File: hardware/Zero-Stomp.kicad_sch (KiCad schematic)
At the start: 90 parts, among them J1 Power, J2 Left Input, J3 Right Input, J4 Expression, J5 Left Output, J6 Right Output, J7 MIDI_IN, J8 MIDI_OUT, U1 L78L05_TO92, U2 H11L1, U3 RP2040-Zero, U4 WM8960CGEFL/V, U5 TL972, U6 SSD1306-OLED-SPI, X1 24MHz

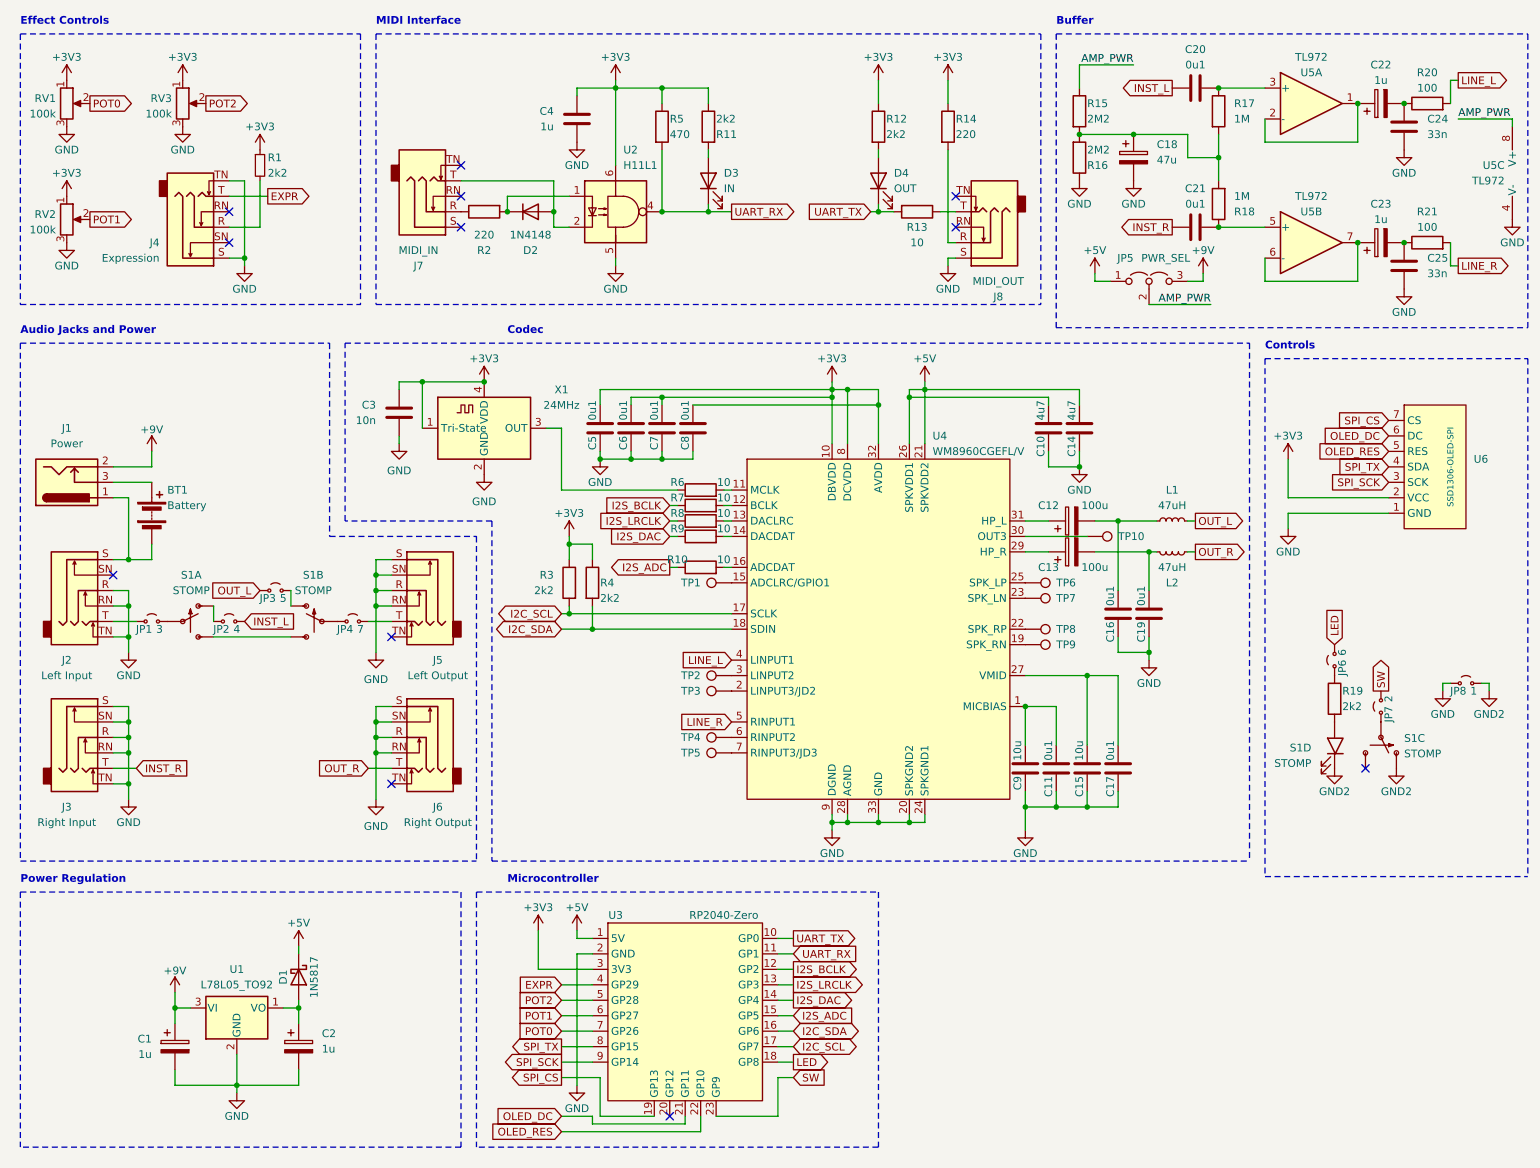
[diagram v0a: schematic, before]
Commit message: Added basic on-board RP2350A to schematic
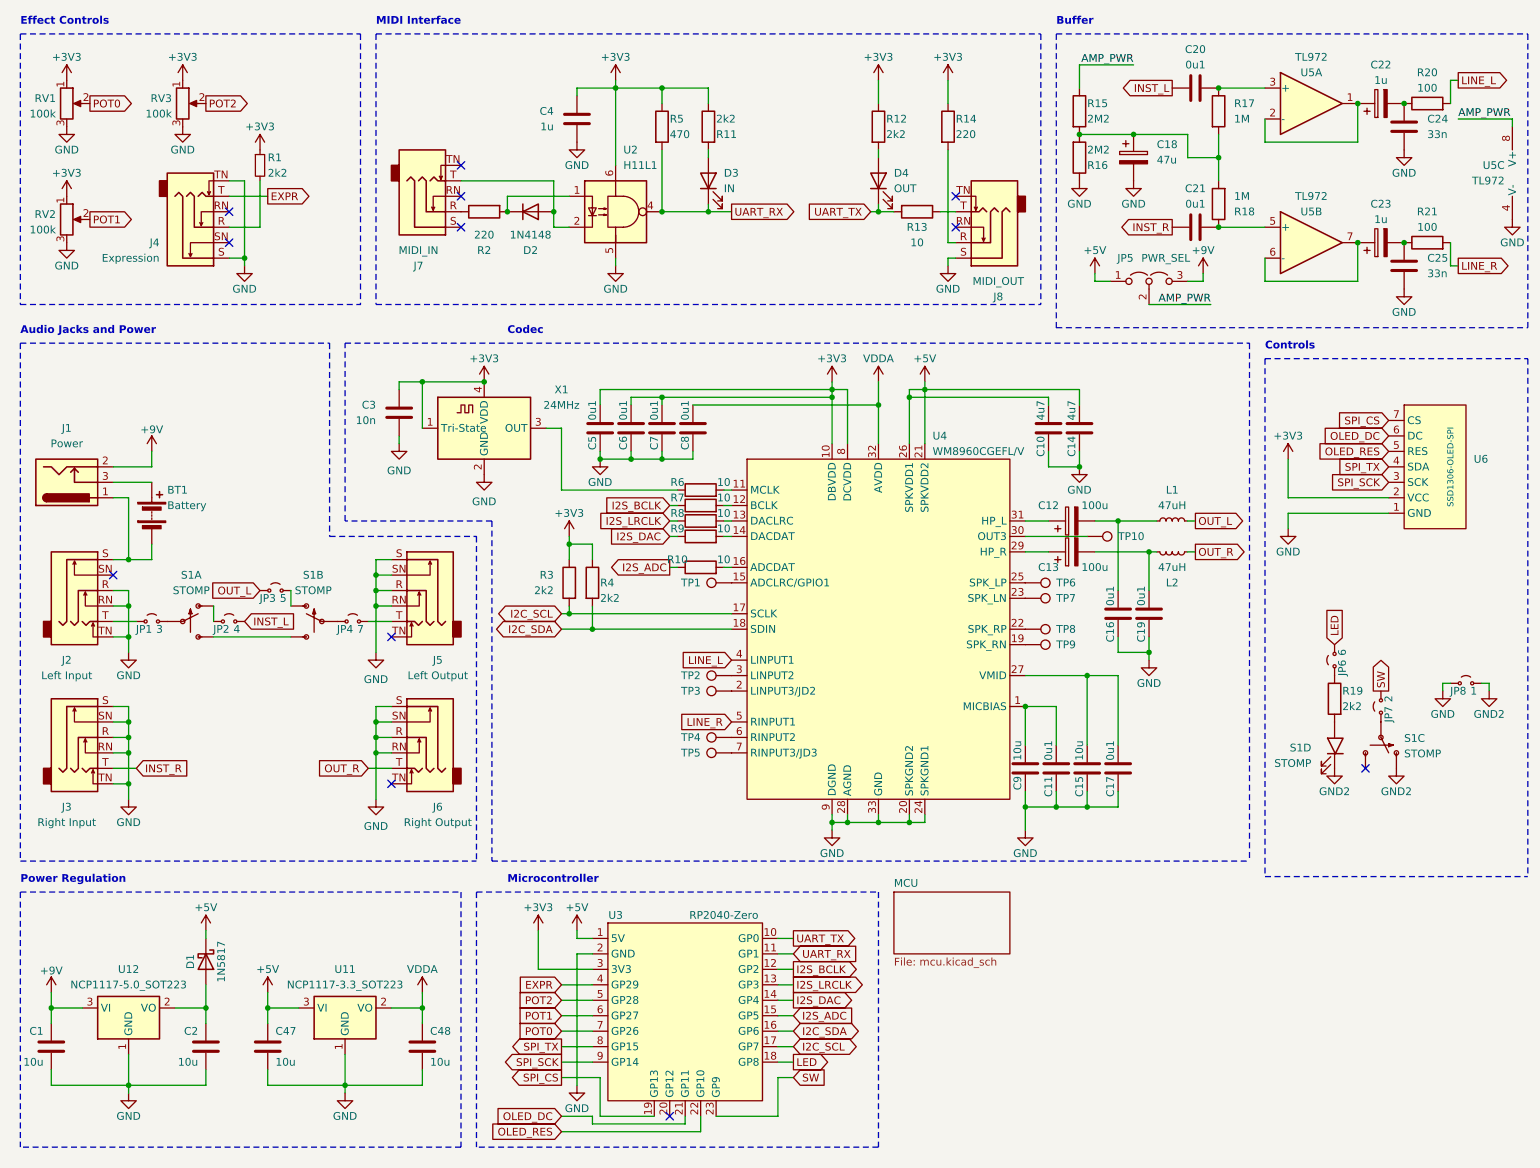
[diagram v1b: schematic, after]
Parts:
- removed C1, C2: 1u, Capacitor_THT:CP_Radial_D5.0mm_P2.00mm, symbol Device:C_Polarized
- removed U1: L78L05_TO92, Package_TO_SOT_THT:TO-92_Inline, symbol Regulator_Linear:L78L05_TO92
- added C1, C2, C47, C48: 10u, symbol Device:C
- added U11: NCP1117-3.3_SOT223, Package_TO_SOT_SMD:SOT-223-3_TabPin2, symbol Regulator_Linear:NCP1117-3.3_SOT223
- added U12: NCP1117-5.0_SOT223, Package_TO_SOT_SMD:SOT-223-3_TabPin2, symbol Regulator_Linear:NCP1117-5.0_SOT223
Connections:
- net +3V3: no longer C8.1, U4.32 (AVDD)
- net +5V: now also C47.1, U11.3 (VI)
- net +9V: now also C1.1, U12.3 (VI)
- net GND: now also C1.2, C2.2, C47.2, C48.2, U11.1 (GND), U12.1 (GND)
- net at D1.2 (A): now also C2.1, U12.2 (VO)
- new net VDDA: C48.1, C8.1, U11.2 (VO), U4.32 (AVDD)
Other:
- added sheet MCU (mcu.kicad_sch)
- moved on the sheet: D1

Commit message: Schematic revision completed
New codec, TLV320AIC3104. Improved power isolation. More control inputs. Modular design.
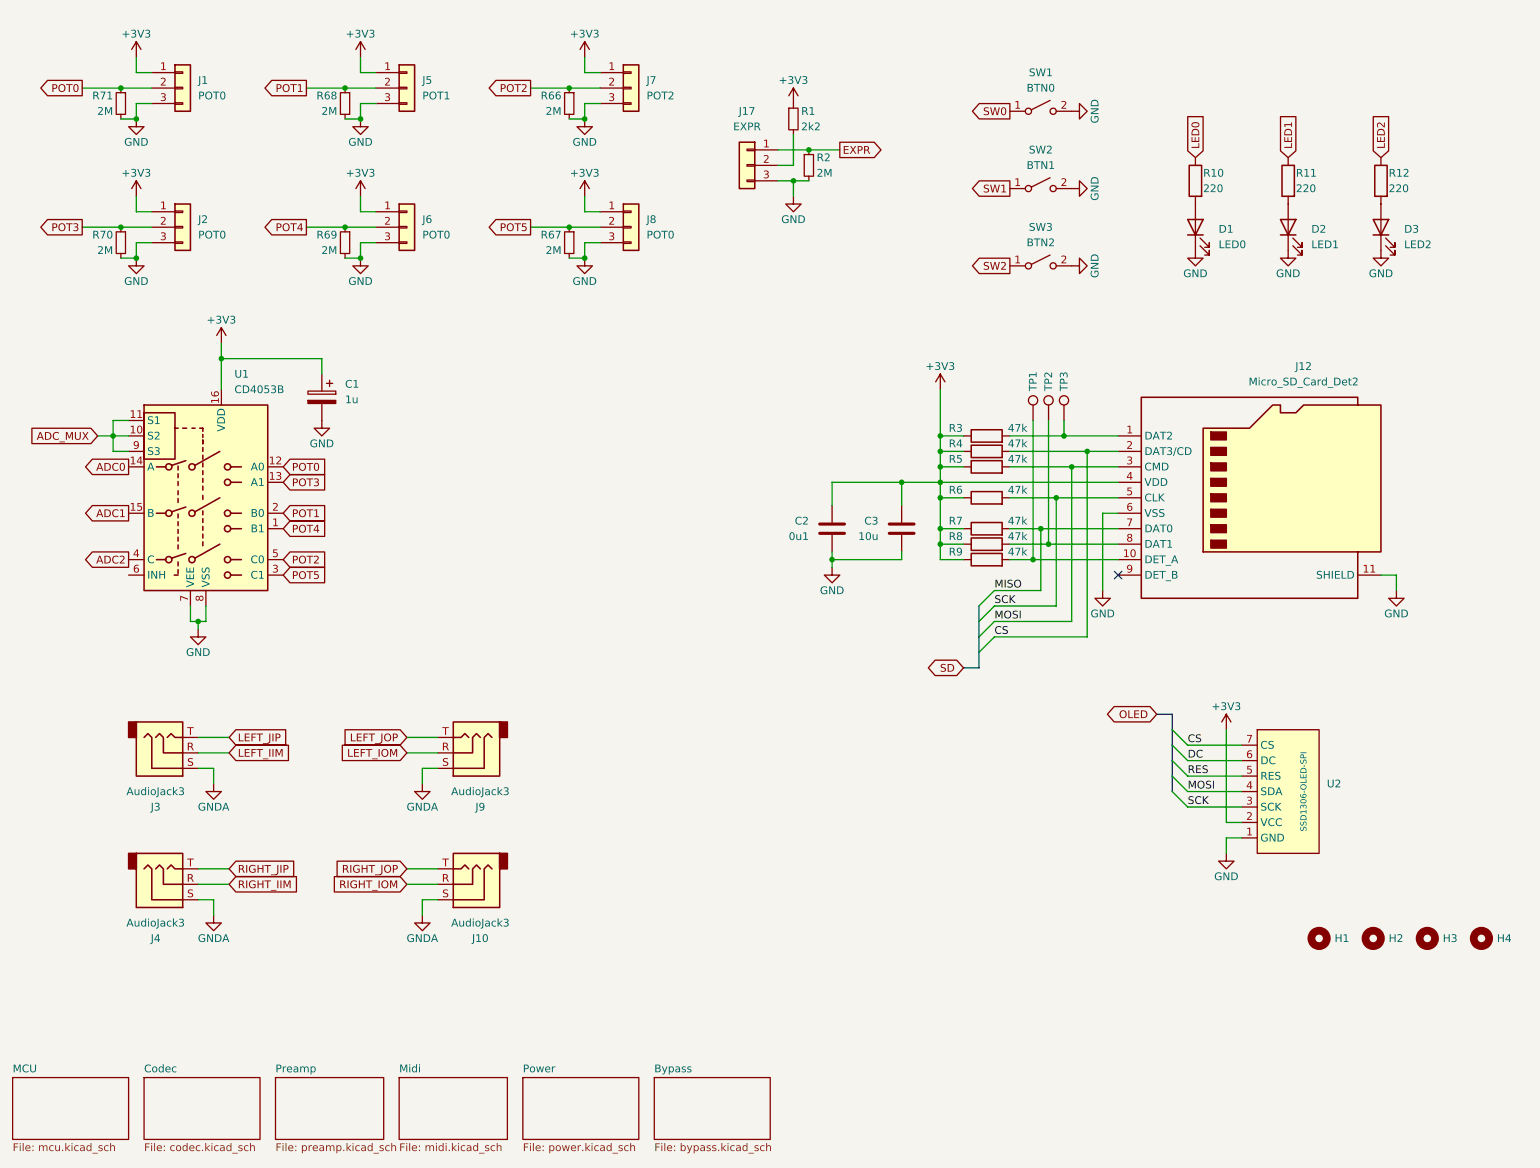
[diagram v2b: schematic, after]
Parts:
- removed BT1: Battery, Connector_PinHeader_2.54mm:PinHeader_1x02_P2.54mm_Vertical, symbol Device:Battery
- removed C1, C47, C48: 10u, symbol Device:C
- removed C10, C14: 4u7, Capacitor_SMD:C_0805_2012Metric_Pad1.18x1.45mm_HandSolder, symbol Device:C
- removed C11, C17, C5, C6, C7, C8: 0u1, Capacitor_SMD:C_0805_2012Metric_Pad1.18x1.45mm_HandSolder, symbol Device:C
- removed C12, C13: 100u, Capacitor_THT:CP_Radial_D6.3mm_P2.50mm, symbol Device:C_Polarized
- removed C15, C9: 10u, Capacitor_SMD:C_0805_2012Metric_Pad1.18x1.45mm_HandSolder, symbol Device:C
- removed C16, C19, C20, C21: 0u1, Capacitor_THT:C_Rect_L4.0mm_W2.5mm_P2.50mm, symbol Device:C
- removed C18: 47u, Capacitor_THT:CP_Radial_D5.0mm_P2.00mm, symbol Device:C_Polarized
- removed C22, C23: 1u, Capacitor_THT:CP_Radial_D5.0mm_P2.00mm, symbol Device:C_Polarized
- removed C24, C25: 33n, Capacitor_THT:C_Rect_L4.0mm_W2.5mm_P2.50mm, symbol Device:C
- removed C4: 1u, Capacitor_THT:C_Rect_L4.0mm_W2.5mm_P2.50mm, symbol Device:C
- removed D1: 1N5817, Diode_THT:D_DO-41_SOD81_P2.54mm_Vertical_AnodeUp, symbol Diode:1N5817
- removed D2: 1N4148, Diode_THT:D_DO-35_SOD27_P2.54mm_Vertical_AnodeUp, symbol Diode:1N4148
- removed D4: OUT, LED_THT:LED_D3.0mm, symbol Device:LED
- removed J1: Power, Connector_BarrelJack:BarrelJack_Horizontal, symbol Connector:Barrel_Jack_Switch
- removed J2: Left Input, Connector_Audio:Jack_6.35mm_Neutrik_NMJ6HFD2_Horizontal, symbol Connector_Audio:AudioJack3_Switch
- removed J3: Right Input, Connector_Audio:Jack_6.35mm_Neutrik_NMJ6HFD2_Horizontal, symbol Connector_Audio:AudioJack3_Switch
- removed J4: Expression, Connector_Audio:Jack_6.35mm_Neutrik_NMJ6HFD2_Horizontal, symbol Connector_Audio:AudioJack3_Switch
- removed J5: Left Output, Connector_Audio:Jack_6.35mm_Neutrik_NMJ6HFD2_Horizontal, symbol Connector_Audio:AudioJack3_Switch
- removed J6: Right Output, Connector_Audio:Jack_6.35mm_Neutrik_NMJ6HFD2_Horizontal, symbol Connector_Audio:AudioJack3_Switch
- removed J7: MIDI_IN, Connector_Audio:Jack_3.5mm_CUI_SJ1-3525N_Horizontal, symbol Connector_Audio:AudioJack3_SwitchTR
- removed J8: MIDI_OUT, Connector_Audio:Jack_3.5mm_CUI_SJ1-3525N_Horizontal, symbol Connector_Audio:AudioJack3_SwitchTR
- removed JP1: 3, Zero-Stomp:Jumper_2_THT_P2.54mm, symbol Jumper:Jumper_2_Small_Open
- removed JP2: 4, Zero-Stomp:Jumper_2_THT_P2.54mm, symbol Jumper:Jumper_2_Small_Open
- removed JP3: 5, Zero-Stomp:Jumper_2_THT_P2.54mm, symbol Jumper:Jumper_2_Small_Open
- removed JP4: 7, Zero-Stomp:Jumper_2_THT_P2.54mm, symbol Jumper:Jumper_2_Small_Open
- removed JP5: PWR_SEL, Connector_PinHeader_2.54mm:PinHeader_1x03_P2.54mm_Vertical, symbol Jumper:Jumper_3_Open
- removed JP6: 6, Zero-Stomp:Jumper_2_THT_P2.54mm, symbol Jumper:Jumper_2_Small_Open
- removed JP7: 2, Zero-Stomp:Jumper_2_THT_P2.54mm, symbol Jumper:Jumper_2_Small_Open
- removed JP8: 1, Zero-Stomp:Jumper_2_THT_P2.54mm, symbol Jumper:Jumper_2_Small_Open
- removed L1, L2: 47uH, Inductor_THT:L_Axial_L6.6mm_D2.7mm_P2.54mm_Vertical_Vishay_IM-2, symbol Device:L_Small
- removed R13: 10, Resistor_THT:R_Axial_DIN0207_L6.3mm_D2.5mm_P2.54mm_Vertical, symbol Device:R
- removed R14, R2: 220, Resistor_THT:R_Axial_DIN0207_L6.3mm_D2.5mm_P2.54mm_Vertical, symbol Device:R
- removed R15, R16: 2M2, Resistor_THT:R_Axial_DIN0207_L6.3mm_D2.5mm_P2.54mm_Vertical, symbol Device:R
- removed R17, R18: 1M, Resistor_THT:R_Axial_DIN0207_L6.3mm_D2.5mm_P2.54mm_Vertical, symbol Device:R
- removed R19: 2k2, Resistor_THT:R_Axial_DIN0207_L6.3mm_D2.5mm_P2.54mm_Vertical, symbol Device:R
- removed R20, R21: 100, Resistor_THT:R_Axial_DIN0207_L6.3mm_D2.5mm_P2.54mm_Vertical, symbol Device:R
- removed RV1, RV2, RV3: 100k, Potentiometer_THT:Potentiometer_Omeg_PC16BU_Vertical, symbol Device:R_Potentiometer
- removed S1: STOMP, Zero-Stomp:STOMP-3PDT-LED, symbol Zero-Stomp:STOMP-3PDT-LED
- removed TP10, TP4, TP5, TP6, TP7, TP8, TP9: TestPoint, TestPoint:TestPoint_Pad_D1.5mm, symbol Connector:TestPoint
- removed U11: NCP1117-3.3_SOT223, Package_TO_SOT_SMD:SOT-223-3_TabPin2, symbol Regulator_Linear:NCP1117-3.3_SOT223
- removed U12: NCP1117-5.0_SOT223, Package_TO_SOT_SMD:SOT-223-3_TabPin2, symbol Regulator_Linear:NCP1117-5.0_SOT223
- removed U2: H11L1, Package_DIP:DIP-6_W7.62mm, symbol Isolator:H11L1
- removed U3: RP2040-Zero, RP2040-Zero:RP2040 Zero, symbol RP2040-Zero:RP2040-Zero
- removed U4: WM8960CGEFL/V, Package_DFN_QFN:QFN-32-1EP_5x5mm_P0.5mm_EP3.3x3.3mm_ThermalVias, symbol Zero-Stomp:WM8960CGEFL/V
- removed U5: TL972, Package_DIP:DIP-8_W7.62mm, symbol Amplifier_Operational:TL072
- removed X1: 24MHz, Oscillator:Oscillator_SMD_ECS_2520MV-xxx-xx-4Pin_2.5x2.0mm, symbol Oscillator:ECS-2520MV-xxx-xx
- added C1: 1u, symbol Device:C_Polarized
- added D1: LED0, symbol Device:LED
- added D2: LED1, symbol Device:LED
- added H1, H2, H3, H4: MountingHole, symbol Mechanical:MountingHole
- added J1, J2, J6, J8: POT0, symbol Connector_Generic:Conn_01x03
- added J10, J3, J4, J9: AudioJack3, symbol Connector_Audio:AudioJack3
- added J12: Micro_SD_Card_Det2, symbol Connector:Micro_SD_Card_Det2
- added J17: EXPR, symbol Connector_Generic:Conn_01x03
- added J5: POT1, symbol Connector_Generic:Conn_01x03
- added J7: POT2, symbol Connector_Generic:Conn_01x03
- added R2, R66, R67, R68, R69, R70, R71: 2M, Resistor_THT:R_Axial_DIN0207_L6.3mm_D2.5mm_P2.54mm_Vertical, symbol Device:R_Small
- added SW1: BTN0, symbol Switch:SW_SPST
- added SW2: BTN1, symbol Switch:SW_SPST
- added SW3: BTN2, symbol Switch:SW_SPST
- added U1: CD4053B, symbol Analog_Switch:CD4053B
- C2: value 10u -> 0u1
- C3: value 10n -> 10u; footprint Capacitor_SMD:C_0805_2012Metric_Pad1.18x1.45mm_HandSolder -> (none)
- D3: value IN -> LED2; footprint LED_THT:LED_D3.0mm -> (none)
- R10: value 10 -> 220; footprint Resistor_SMD:R_0805_2012Metric_Pad1.20x1.40mm_HandSolder -> Resistor_THT:R_Axial_DIN0207_L6.3mm_D2.5mm_P2.54mm_Vertical
- R11, R12: value 2k2 -> 220
- R3, R4: value 2k2 -> 47k; footprint Resistor_SMD:R_0805_2012Metric_Pad1.20x1.40mm_HandSolder -> (none)
- R5: value 470 -> 47k; footprint Resistor_THT:R_Axial_DIN0207_L6.3mm_D2.5mm_P2.54mm_Vertical -> (none)
- R6, R7, R8, R9: value 10 -> 47k; footprint Resistor_SMD:R_0805_2012Metric_Pad1.20x1.40mm_HandSolder -> (none)
- TP1, TP2, TP3: footprint TestPoint:TestPoint_Pad_D1.5mm -> (none)
- renumbered U6 to U2
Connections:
- net I2C_SCL is gone; now on an unnamed net: R3.2
- net I2S_BCLK is gone; now on net +3V3: R7.1
- net I2S_DAC is gone; now on net +3V3: R9.1
- net I2S_LRCLK is gone; now on net +3V3: R8.1
- net SPI_CS is gone; now on net CS: U2.7 (CS)
- net SPI_SCK is gone; now on net SCK: U2.3 (SCK)
- net +3V3: now also C2.1, R6.1, C1.1, J1.1 (Pin_1), J12.4 (VDD), J2.1 (Pin_1), J5.1 (Pin_1), J6.1 (Pin_1), J7.1 (Pin_1), J8.1 (Pin_1), U1.16 (VDD); no longer R11.1, R12.1
- net EXPR: now also J17.1 (Pin_1), R2.1
- net GND: now also D3.1 (K), C1.2, D1.1 (K), D2.1 (K), J1.3 (Pin_3), J12.11 (SHIELD), J12.6 (VSS), J17.3 (Pin_3), J2.3 (Pin_3), J5.3 (Pin_3), J6.3 (Pin_3), J7.3 (Pin_3), J8.3 (Pin_3), R2.2, R66.2, R67.2, R68.2, R69.2, R70.2, R71.2, SW1.2 (B), SW2.2 (B), SW3.2 (B), U1.7 (VEE), U1.8 (VSS)
- net POT0: now also J1.2 (Pin_2), R71.1, U1.12 (A0)
- net POT1: now also J5.2 (Pin_2), R68.1, U1.2 (B0)
- net POT2: now also J7.2 (Pin_2), R66.1, U1.5 (C0)
- net at R8.2: now also TP2.1, J12.8 (DAT1)
- net at R9.2: now also TP1.1, J12.10 (DET_A)
- net at R1.2: now also J17.2 (Pin_2)
- net SCK: now reaches R6.2
- net SCK: now also J12.5 (CLK)
- net MISO: now reaches R7.2
- net MISO: now also J12.7 (DAT0)
- net at R10.2: now also D1.2 (A)
- net at TP3.1: now also J12.1 (DAT2)
- net at R11.2: now also D2.2 (A); no longer D3.2 (A)
- net at R12.2: now also D3.2 (A)
- net I2C_SDA renamed CS
- net CS: now also J12.2 (DAT3/CD)
- net I2S_ADC renamed LED0
- net OLED_DC renamed DC
- net OLED_RES renamed RES
- net SPI_TX renamed MOSI
- net MOSI: now also R5.2, J12.3 (CMD)
- removed net UART_RX: D3.1 (K), R5.2
- new net ADC0: U1.14 (A)
- new net ADC1: U1.15 (B)
- new net ADC2: U1.4 (C)
- new net ADC_MUX: U1.10 (S2), U1.11 (S1), U1.9 (S3)
- new net GNDA: J10.S, J3.S, J4.S, J9.S
- new net LED1: R11.1
- new net LED2: R12.1
- new net LEFT_IIM: J3.R
- new net LEFT_IOM: J9.R
- new net LEFT_JIP: J3.T
- new net LEFT_JOP: J9.T
- new net POT3: J2.2 (Pin_2), R70.1, U1.13 (A1)
- new net POT4: J6.2 (Pin_2), R69.1, U1.1 (B1)
- new net POT5: J8.2 (Pin_2), R67.1, U1.3 (C1)
- new net RIGHT_IIM: J4.R
- new net RIGHT_IOM: J10.R
- new net RIGHT_JIP: J4.T
- new net RIGHT_JOP: J10.T
- new net SW0: SW1.1 (A)
- new net SW1: SW2.1 (A)
- new net SW2: SW3.1 (A)
- no-connect marks 12 -> 1
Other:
- added sheet Bypass (bypass.kicad_sch)
- added sheet Codec (codec.kicad_sch)
- added sheet Midi (midi.kicad_sch)
- added sheet Power (power.kicad_sch)
- added sheet Preamp (preamp.kicad_sch)
- note removed: "Audio Jacks and Power"
- note removed: "Buffer"
- note removed: "Codec"
- note removed: "Controls"
- note removed: "Effect Controls"
- note removed: "MIDI Interface"
- note removed: "Microcontroller"
- note removed: "Power Regulation"
- moved on the sheet: R1, U2

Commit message: Reset references and remove THT footprint assignments.
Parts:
- removed C1: 1u, symbol Device:C_Polarized
- added C1: 1u, Capacitor_SMD:C_01005_0402Metric, symbol Device:C
- R1: renamed from R71; footprint Resistor_THT:R_Axial_DIN0207_L6.3mm_D2.5mm_P2.54mm_Vertical -> (none)
- R16: renamed from R10; footprint Resistor_THT:R_Axial_DIN0207_L6.3mm_D2.5mm_P2.54mm_Vertical -> (none)
- R17: renamed from R11; footprint Resistor_THT:R_Axial_DIN0207_L6.3mm_D2.5mm_P2.54mm_Vertical -> (none)
- R18: renamed from R12; footprint Resistor_THT:R_Axial_DIN0207_L6.3mm_D2.5mm_P2.54mm_Vertical -> (none)
- R2: renamed from R70; footprint Resistor_THT:R_Axial_DIN0207_L6.3mm_D2.5mm_P2.54mm_Vertical -> (none)
- R3: renamed from R68; footprint Resistor_THT:R_Axial_DIN0207_L6.3mm_D2.5mm_P2.54mm_Vertical -> (none)
- R4: renamed from R69; footprint Resistor_THT:R_Axial_DIN0207_L6.3mm_D2.5mm_P2.54mm_Vertical -> (none)
- R5: renamed from R66; footprint Resistor_THT:R_Axial_DIN0207_L6.3mm_D2.5mm_P2.54mm_Vertical -> (none)
- R6: renamed from R67; footprint Resistor_THT:R_Axial_DIN0207_L6.3mm_D2.5mm_P2.54mm_Vertical -> (none)
- R7: renamed from R1; footprint Resistor_THT:R_Axial_DIN0207_L6.3mm_D2.5mm_P2.54mm_Vertical -> (none)
- R8: renamed from R2; footprint Resistor_THT:R_Axial_DIN0207_L6.3mm_D2.5mm_P2.54mm_Vertical -> (none)
- renumbered J3 to J1, J8 to J10, J17 to J11, J4 to J2, J1 to J3, J2 to J4, J9 to J7, J10 to J8, J7 to J9, R4 to R10, R5 to R11, R6 to R12, R7 to R13, R8 to R14, R9 to R15, R3 to R9
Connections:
- net +3V3: now also C1.1
- net GND: now also C1.2

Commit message: Footprint assignments
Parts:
- removed J10, J3, J4, J6: POT0, symbol Connector_Generic:Conn_01x03
- removed J11: EXPR, symbol Connector_Generic:Conn_01x03
- removed J12: Micro_SD_Card_Det2, symbol Connector:Micro_SD_Card_Det2
- removed J5: POT1, symbol Connector_Generic:Conn_01x03
- removed J9: POT2, symbol Connector_Generic:Conn_01x03
- added J11: EXPR, Connector_JST:JST_PH_B3B-PH-K_1x03_P2.00mm_Vertical, symbol Connector_Audio:AudioJack3
- added J6: Micro_SD_Card_Det1, Zero-Stomp:Xunpu_TF-115_microSD, symbol Connector:Micro_SD_Card_Det1
- added RV1: POT0, Connector_JST:JST_PH_B3B-PH-K_1x03_P2.00mm_Vertical, symbol Device:R_Potentiometer
- added RV2: POT1, Connector_JST:JST_PH_B3B-PH-K_1x03_P2.00mm_Vertical, symbol Device:R_Potentiometer
- added RV3: POT2, Connector_JST:JST_PH_B3B-PH-K_1x03_P2.00mm_Vertical, symbol Device:R_Potentiometer
- added RV4: POT3, Connector_JST:JST_PH_B3B-PH-K_1x03_P2.00mm_Vertical, symbol Device:R_Potentiometer
- added RV5: POT4, Connector_JST:JST_PH_B3B-PH-K_1x03_P2.00mm_Vertical, symbol Device:R_Potentiometer
- added RV6: POT5, Connector_JST:JST_PH_B3B-PH-K_1x03_P2.00mm_Vertical, symbol Device:R_Potentiometer
- C1: footprint Capacitor_SMD:C_01005_0402Metric -> Capacitor_SMD:C_0603_1608Metric
- C2: footprint (none) -> Capacitor_SMD:C_0402_1005Metric
- C3: footprint (none) -> Capacitor_SMD:C_0603_1608Metric
- D1, D2, D3: footprint (none) -> Connector_PinSocket_2.54mm:PinSocket_1x02_P2.54mm_Vertical
- H1, H2, H3, H4: footprint (none) -> MountingHole:MountingHole_3.2mm_M3
- J1: value AudioJack3 -> LEFT_IN; footprint (none) -> Connector_JST:JST_PH_B3B-PH-K_1x03_P2.00mm_Vertical
- J2: value AudioJack3 -> RIGHT_IN; footprint (none) -> Connector_JST:JST_PH_B3B-PH-K_1x03_P2.00mm_Vertical
- J7: value AudioJack3 -> LEFT_OUT; footprint (none) -> Connector_JST:JST_PH_B3B-PH-K_1x03_P2.00mm_Vertical
- J8: value AudioJack3 -> RIGHT_OUT; footprint (none) -> Connector_JST:JST_PH_B3B-PH-K_1x03_P2.00mm_Vertical
- R1, R2, R3, R4, R5, R6, R7, R8: footprint (none) -> Resistor_SMD:R_0603_1608Metric
- R10, R11, R12, R13, R14, R15, R9: footprint (none) -> Resistor_SMD:R_0402_1005Metric
- R16, R17, R18: footprint (none) -> Resistor_SMD:R_0805_2012Metric
- SW1, SW2, SW3: footprint (none) -> Connector_JST:JST_PH_B2B-PH-K_1x02_P2.00mm_Vertical
- TP1, TP2, TP3: footprint (none) -> TestPoint:TestPoint_Pad_D1.0mm
- U1: footprint (none) -> Package_SO:SOIC-16_3.9x9.9mm_P1.27mm
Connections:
- net +3V3: now also J6.4 (VDD), RV1.1, RV2.1, RV3.1, RV4.1, RV5.1, RV6.1
- net CS: now also J6.2 (DAT3/CD)
- net EXPR: now also J11.T
- net GND: now also J11.S, J6.10 (SHIELD), J6.6 (VSS), RV1.3, RV2.3, RV3.3, RV4.3, RV5.3, RV6.3
- net MISO: now also J6.7 (DAT0)
- net MOSI: now also J6.3 (CMD)
- net POT0: now also RV1.2
- net POT1: now also RV2.2
- net POT2: now also RV3.2
- net POT3: now also RV4.2
- net POT4: now also RV5.2
- net POT5: now also RV6.2
- net SCK: now also J6.5 (CLK)
- net at R7.2: now also J11.R
- net at R14.2, TP2.1: now also J6.8 (DAT1)
- net at R15.2, TP1.1: now also J6.9 (DET)
- net at R9.2, TP3.1: now also J6.1 (DAT2)
- no-connect marks 1 -> 0
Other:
- moved on the sheet: R1, R15
